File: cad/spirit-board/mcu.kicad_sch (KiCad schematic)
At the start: 6 parts, among them IC1 BLUENRG-M2SA, J1 Conn_ARM_JTAG_SWD_10, J2 Conn_01x03_Pin

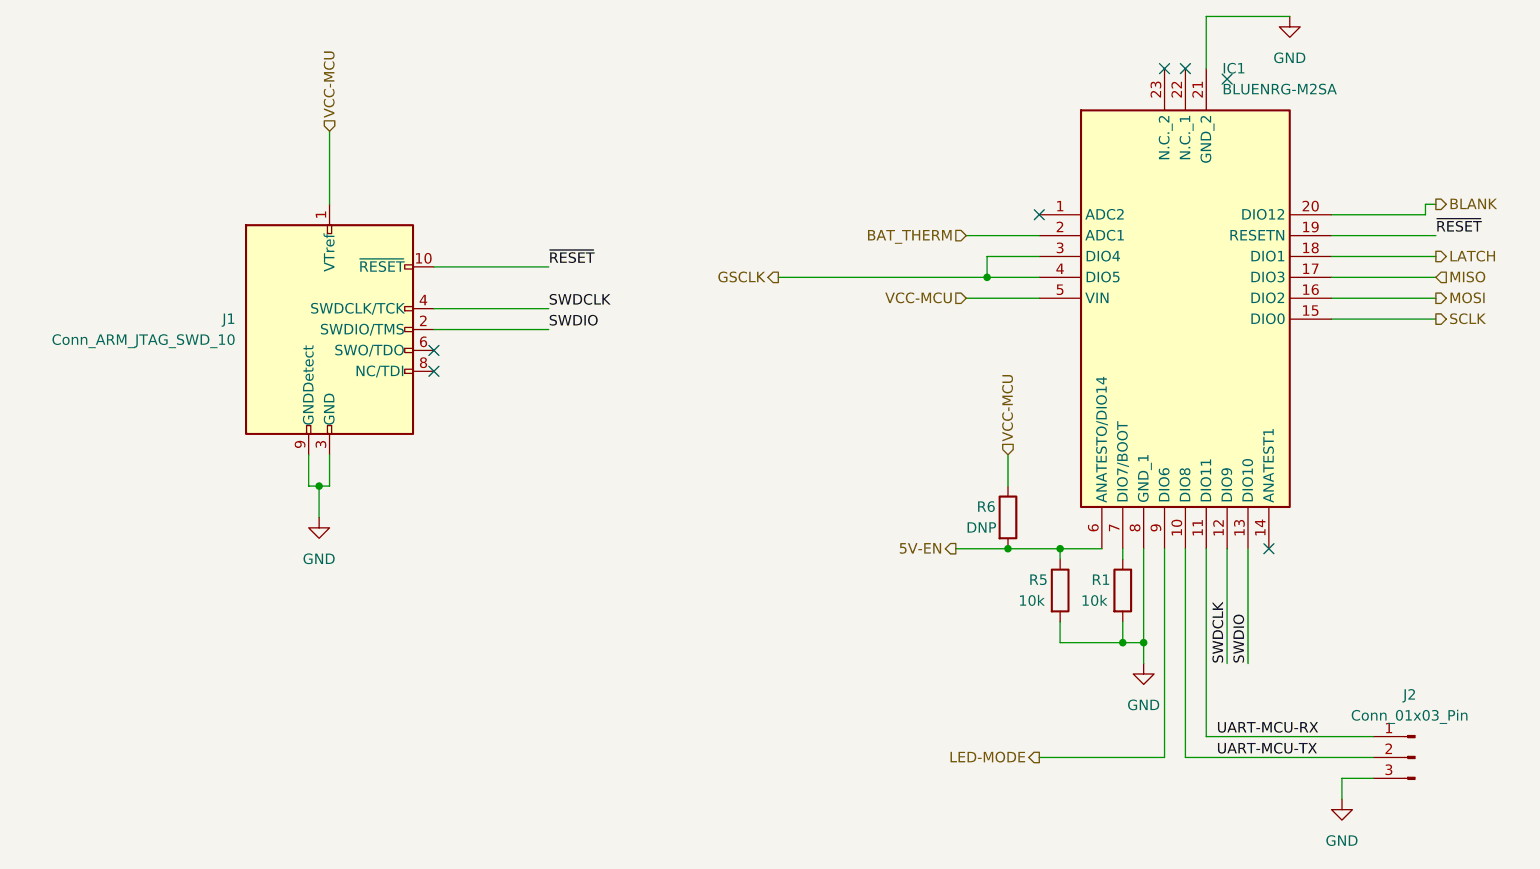
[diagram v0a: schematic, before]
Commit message: Mike's feedback
 - bypass caps on all power sources
 - Bulk cap on LED power
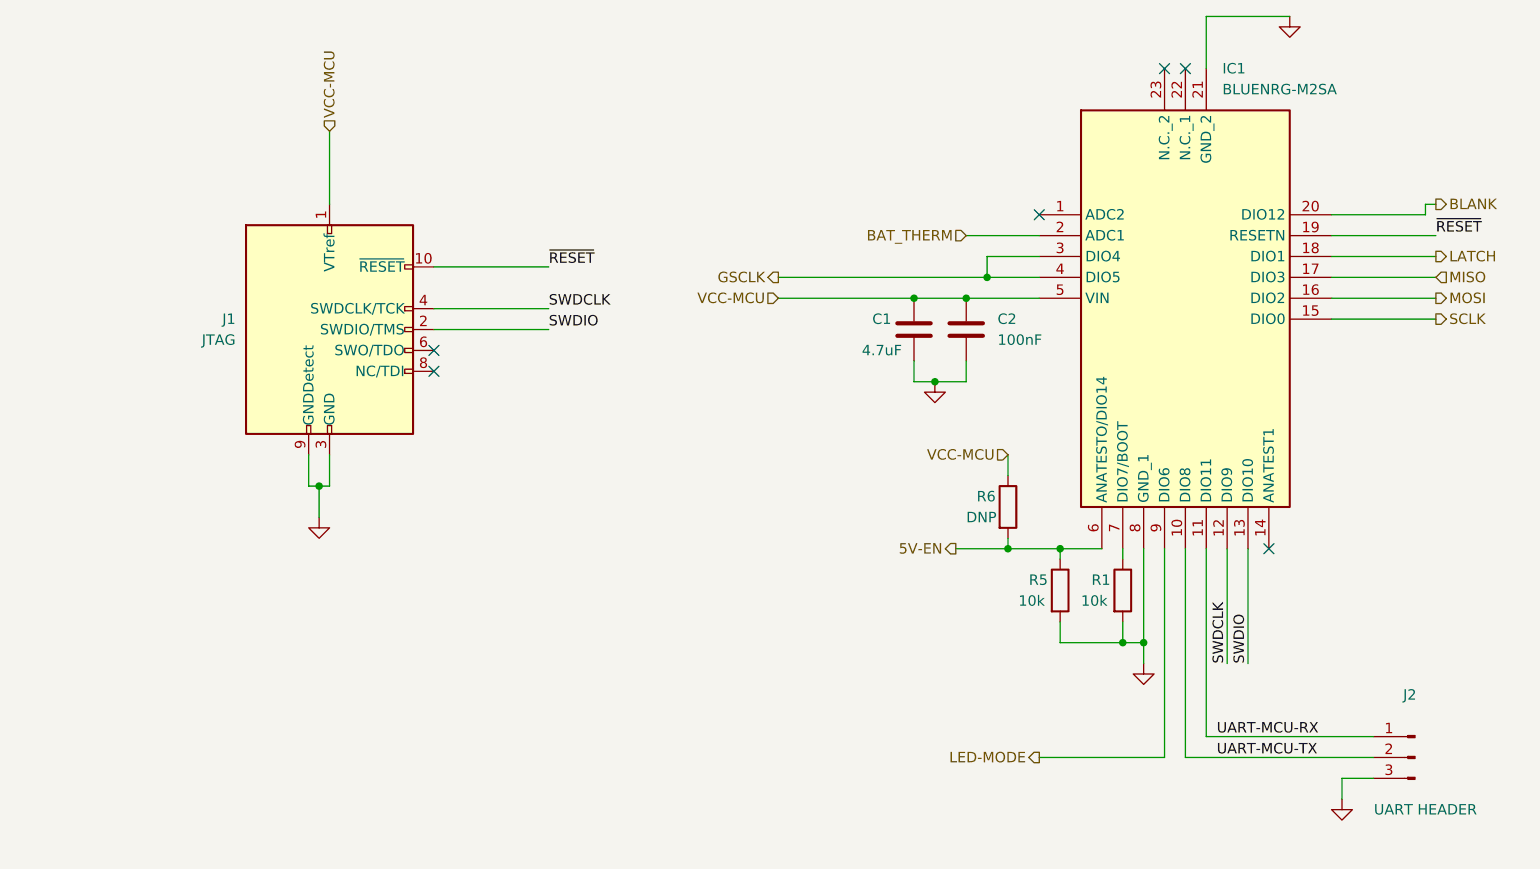
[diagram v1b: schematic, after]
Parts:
- added C1: 4.7uF, symbol Device:C
- added C2: 100nF, symbol Device:C
- J1: value Conn_ARM_JTAG_SWD_10 -> JTAG
- J2: value Conn_01x03_Pin -> UART HEADER
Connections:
- net GND: now also C1.2, C2.2
- net VCC-MCU: now also C1.1, C2.1
- no-connect marks 7 -> 6
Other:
- moved on the sheet: R6
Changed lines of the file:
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@@
   (junction (at 172.72 69.85) (diameter 0) (color 0 0 0 0)
   )
+  (junction (at 166.37 82.55) (diameter 0) (color 0 0 0 0)
+  )
   (junction (at 191.77 114.3) (diameter 0) (color 0 0 0 0)
   )
   (junction (at 91.44 95.25) (diameter 0) (color 0 0 0 0)
   )
+  (junction (at 170.18 72.39) (diameter 0) (color 0 0 0 0)
+  )
   (junction (at 189.23 114.3) (diameter 0) (color 0 0 0 0)
   )
   (junction (at 175.26 102.87) (diameter 0) (color 0 0 0 0)
+  )
+  (junction (at 163.83 72.39) (diameter 0) (color 0 0 0 0)
   )
   (no_connect (at 196.85 44.45))
@@
   (no_connect (at 194.31 44.45))
   (no_connect (at 105.41 81.28))
-  (no_connect (at 201.93 45.72))
   (no_connect (at 105.41 78.74))
   (wire (pts (xy 92.71 52.07) (xy 92.71 60.96))
@@
     (stroke (width 0) (type default))
   )
+  (wire (pts (xy 170.18 82.55) (xy 170.18 80.01))
+    (stroke (width 0) (type default))
+  )
   (wire (pts (xy 172.72 67.31) (xy 179.07 67.31))
     (stroke (width 0) (type default))
@@
     (stroke (width 0) (type default))
   )
-  (wire (pts (xy 175.26 91.44) (xy 175.26 95.25))
+  (wire (pts (xy 175.26 91.44) (xy 175.26 93.98))
     (stroke (width 0) (type default))
   )
@@
     (stroke (width 0) (type default))
   )
+  (wire (pts (xy 166.37 82.55) (xy 170.18 82.55))
+    (stroke (width 0) (type default))
+  )
   (wire (pts (xy 226.06 60.96) (xy 227.33 60.96))
     (stroke (width 0) (type default))
@@
     (stroke (width 0) (type default))
   )
+  (wire (pts (xy 163.83 72.39) (xy 170.18 72.39))
+    (stroke (width 0) (type default))
+  )
   (wire (pts (xy 189.23 102.87) (xy 189.23 104.14))
     (stroke (width 0) (type default))
@@
     (stroke (width 0) (type default))
   )
+  (wire (pts (xy 175.26 101.6) (xy 175.26 102.87))
+    (stroke (width 0) (type default))
+  )
   (wire (pts (xy 175.26 102.87) (xy 181.61 102.87))
     (stroke (width 0) (type default))
@@
     (stroke (width 0) (type default))
   )
+  (wire (pts (xy 163.83 80.01) (xy 163.83 82.55))
+    (stroke (width 0) (type default))
+  )
   (wire (pts (xy 91.44 95.25) (xy 90.17 95.25))
     (stroke (width 0) (type default))
@@
     (stroke (width 0) (type default))
   )
+  (wire (pts (xy 147.32 72.39) (xy 163.83 72.39))
+    (stroke (width 0) (type default))
+  )
+  (wire (pts (xy 163.83 82.55) (xy 166.37 82.55))
+    (stroke (width 0) (type default))
+  )
+  (wire (pts (xy 214.63 69.85) (xy 227.33 69.85))
+    (stroke (width 0) (type default))
+  )
+  (wire (pts (xy 214.63 74.93) (xy 227.33 74.93))
+    (stroke (width 0) (type default))
+  )
+  (wire (pts (xy 181.61 114.3) (xy 189.23 114.3))
+    (stroke (width 0) (type default))
+  )
   (wire (pts (xy 170.18 72.39) (xy 179.07 72.39))
-    (stroke (width 0) (type default))
-  )
-  (wire (pts (xy 214.63 69.85) (xy 227.33 69.85))
-    (stroke (width 0) (type default))
-  )
-  (wire (pts (xy 214.63 74.93) (xy 227.33 74.93))
-    (stroke (width 0) (type default))
-  )
-  (wire (pts (xy 181.61 114.3) (xy 189.23 114.3))
     (stroke (width 0) (type default))
   )
@@
     (effects (font (size 1.27 1.27)) (justify left bottom))
   )
-  (hierarchical_label "VCC-MCU" (shape input) (at 170.18 72.39 180) (fields_autoplaced)
+  (hierarchical_label "VCC-MCU" (shape input) (at 147.32 72.39 180) (fields_autoplaced)
     (effects (font (size 1.27 1.27)) (justify right))
   )
@@
     (effects (font (size 1.27 1.27)) (justify left))
   )
-  (hierarchical_label "VCC-MCU" (shape input) (at 175.26 91.44 90) (fields_autoplaced)
-    (effects (font (size 1.27 1.27)) (justify left))
+  (hierarchical_label "VCC-MCU" (shape input) (at 175.26 91.44 180) (fields_autoplaced)
+    (effects (font (size 1.27 1.27)) (justify right))
   )
   (hierarchical_label "BAT_THERM" (shape input) (at 170.18 64.77 180) (fields_autoplaced)
@@
     )
     (property "Value" "GND" (at 209.55 43.18 0)
-      (effects (font (size 1.27 1.27)))
+      (effects (font (size 1.27 1.27)) hide)
     )
     (property "Footprint" "" (at 209.55 38.1 0)
@@
         (path "/f49c12c3-b220-4144-8b1f-2e0968189b6f/f190c333-cd82-4178-b85c-c6421439c68f"
           (reference "#PWR03") (unit 1)
+        )
+      )
+    )
+  )
+  (symbol (lib_id "power:GND") (at 166.37 82.55 0) (unit 1)
+    (in_bom yes) (on_board yes) (dnp no) (fields_autoplaced)
+    (property "Reference" "#PWR02" (at 166.37 88.9 0)
+      (effects (font (size 1.27 1.27)) hide)
+    )
+    (property "Value" "GND" (at 166.37 87.63 0)
+      (effects (font (size 1.27 1.27)) hide)
+    )
+    (property "Footprint" "" (at 166.37 82.55 0)
+      (effects (font (size 1.27 1.27)) hide)
+    )
+    (property "Datasheet" "" (at 166.37 82.55 0)
+      (effects (font (size 1.27 1.27)) hide)
+    )
+    (pin "1")
+    (instances
+      (project "spirit-board"
+        (path "/f49c12c3-b220-4144-8b1f-2e0968189b6f"
+          (reference "#PWR02") (unit 1)
+        )
+        (path "/f49c12c3-b220-4144-8b1f-2e0968189b6f/f190c333-cd82-4178-b85c-c6421439c68f"
+          (reference "#PWR016") (unit 1)
         )
       )
@@
     )
     (property "Value" "GND" (at 215.9 138.43 0)
-      (effects (font (size 1.27 1.27)))
+      (effects (font (size 1.27 1.27)) hide)
     )
     (property "Footprint" "" (at 215.9 133.35 0)
@@
     )
     (property "Value" "GND" (at 191.77 121.92 0)
-      (effects (font (size 1.27 1.27)))
+      (effects (font (size 1.27 1.27)) hide)
     )
     (property "Footprint" "" (at 191.77 116.84 0)
@@
     )
   )
-  (symbol (lib_id "Device:R") (at 175.26 99.06 0) (unit 1)
+  (symbol (lib_id "Device:R") (at 175.26 97.79 0) (unit 1)
     (in_bom yes) (on_board yes) (dnp no)
-    (property "Reference" "R6" (at 171.45 97.79 0)
+    (property "Reference" "R6" (at 171.45 96.52 0)
       (effects (font (size 1.27 1.27)) (justify left))
     )
-    (property "Value" "DNP" (at 170.18 100.33 0)
+    (property "Value" "DNP" (at 170.18 99.06 0)
       (effects (font (size 1.27 1.27)) (justify left))
     )
-    (property "Footprint" "" (at 173.482 99.06 90)
-      (effects (font (size 1.27 1.27)) hide)
-    )
-    (property "Datasheet" "~" (at 175.26 99.06 0)
+    (property "Footprint" "" (at 173.482 97.79 90)
+      (effects (font (size 1.27 1.27)) hide)
+    )
+    (property "Datasheet" "~" (at 175.26 97.79 0)
       (effects (font (size 1.27 1.27)) hide)
     )
@@
     )
     (property "Value" "GND" (at 91.44 104.14 0)
-      (effects (font (size 1.27 1.27)))
+      (effects (font (size 1.27 1.27)) hide)
     )
     (property "Footprint" "" (at 91.44 99.06 0)
@@
       (effects (font (size 1.27 1.27)))
     )
-    (property "Value" "Conn_01x03_Pin" (at 224.155 123.19 0)
+    (property "Value" "UART HEADER" (at 226.06 134.62 0)
       (effects (font (size 1.27 1.27)))
     )
@@
       (effects (font (size 1.27 1.27)) (justify right))
     )
-    (property "Value" "Conn_ARM_JTAG_SWD_10" (at 81.28 77.47 0)
+    (property "Value" "JTAG" (at 81.28 77.47 0)
       (effects (font (size 1.27 1.27)) (justify right))
     )
@@
         )
       )
+    )
+  )
+  (symbol (lib_id "Device:C") (at 163.83 76.2 0) (unit 1)
+    (in_bom yes) (on_board yes) (dnp no)
+    (property "Reference" "C1" (at 158.75 74.93 0)
+      (effects (font (size 1.27 1.27)) (justify left))
+    )
+    (property "Value" "4.7uF" (at 157.48 78.74 0)
+      (effects (font (size 1.27 1.27)) (justify left))
+    )
+    (property "Footprint" "" (at 164.7952 80.01 0)
+      (effects (font (size 1.27 1.27)) hide)
+    )
+    (property "Datasheet" "~" (at 163.83 76.2 0)
+      (effects (font (size 1.27 1.27)) hide)
+    )
+    (pin "1")
+    (pin "2")
+    (instances
+      (project "spirit-board"
+        (path "/f49c12c3-b220-4144-8b1f-2e0968189b6f/f190c333-cd82-4178-b85c-c6421439c68f"
+          (reference "C1") (unit 1)
+        )
+      )
+    )
+  )
+  (symbol (lib_id "Device:C") (at 170.18 76.2 0) (unit 1)
+    (in_bom yes) (on_board yes) (dnp no) (fields_autoplaced)
+    (property "Reference" "C2" (at 173.99 74.93 0)
+      (effects (font (size 1.27 1.27)) (justify left))
+    )
+    (property "Value" "100nF" (at 173.99 77.47 0)
+      (effects (font (size 1.27 1.27)) (justify left))
+    )
+    (property "Footprint" "" (at 171.1452 80.01 0)
+      (effects (font (size 1.27 1.27)) hide)
+    )
+    (property "Datasheet" "~" (at 170.18 76.2 0)
+      (effects (font (size 1.27 1.27)) hide)
+    )
+    (pin "1")
+    (pin "2")
+    (instances
+      (project "spirit-board"
+        (path "/f49c12c3-b220-4144-8b1f-2e0968189b6f/f190c333-cd82-4178-b85c-c6421439c68f"
+          (reference "C2") (unit 1)
+        )
+      )
